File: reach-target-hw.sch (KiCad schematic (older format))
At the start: 37 parts, among them U1 nRF51822-QF, X1 16MHz 40ppm, X2 32.768kHz 20ppm

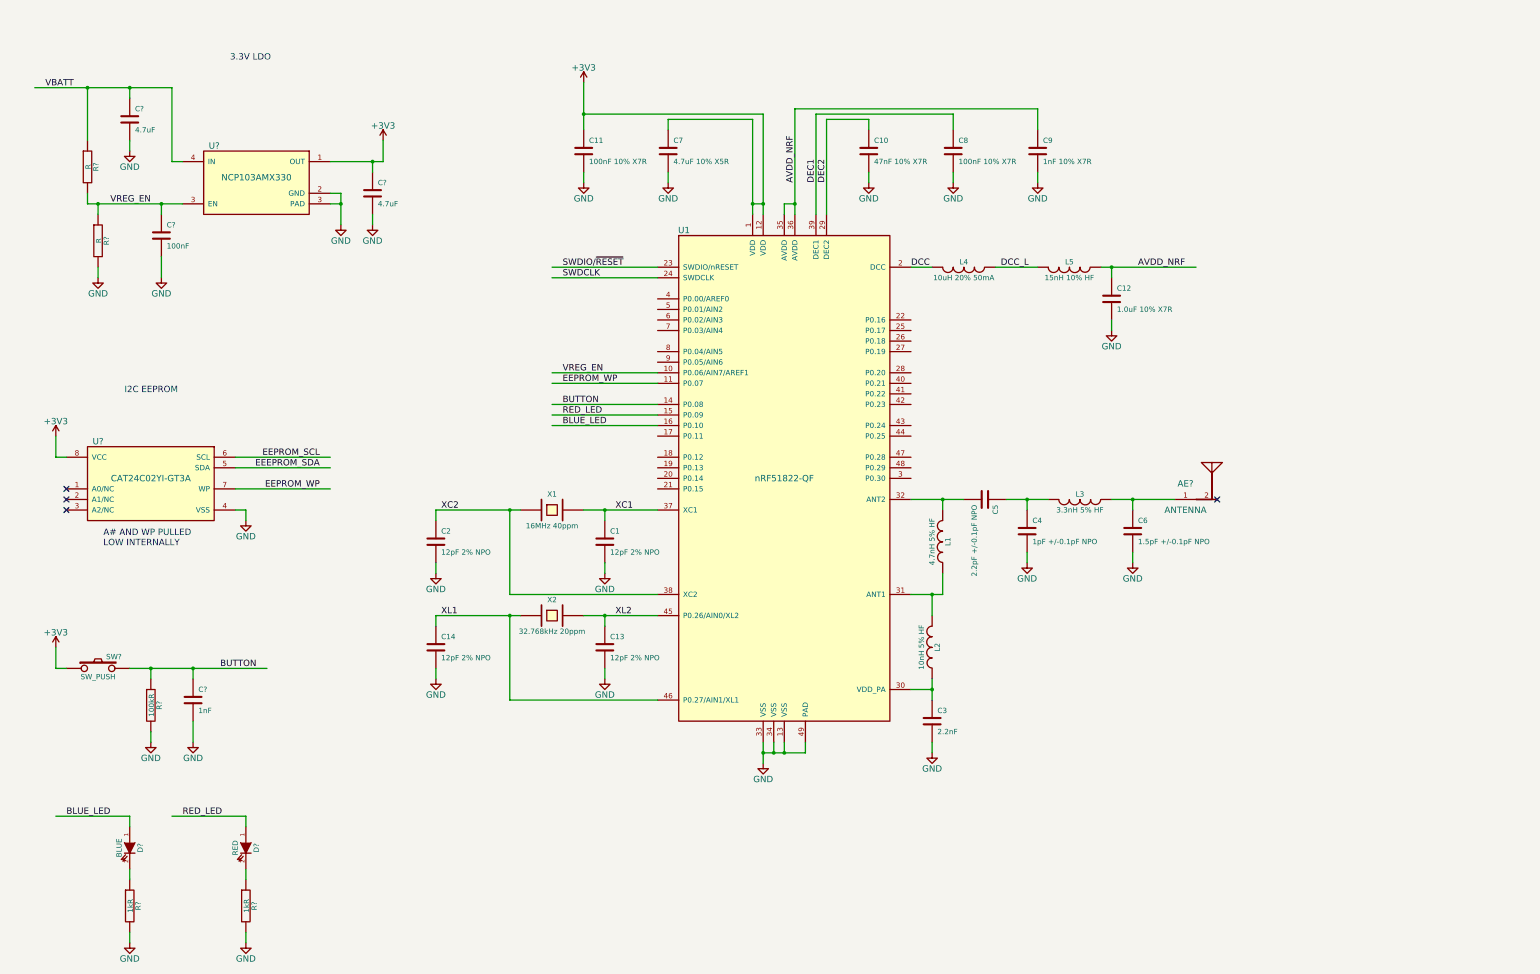
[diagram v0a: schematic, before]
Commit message: added swd/cortex debug pinout. related: none of the nordic reference designs are useful...stupid debugger/usb-to-serial micros are in the way.
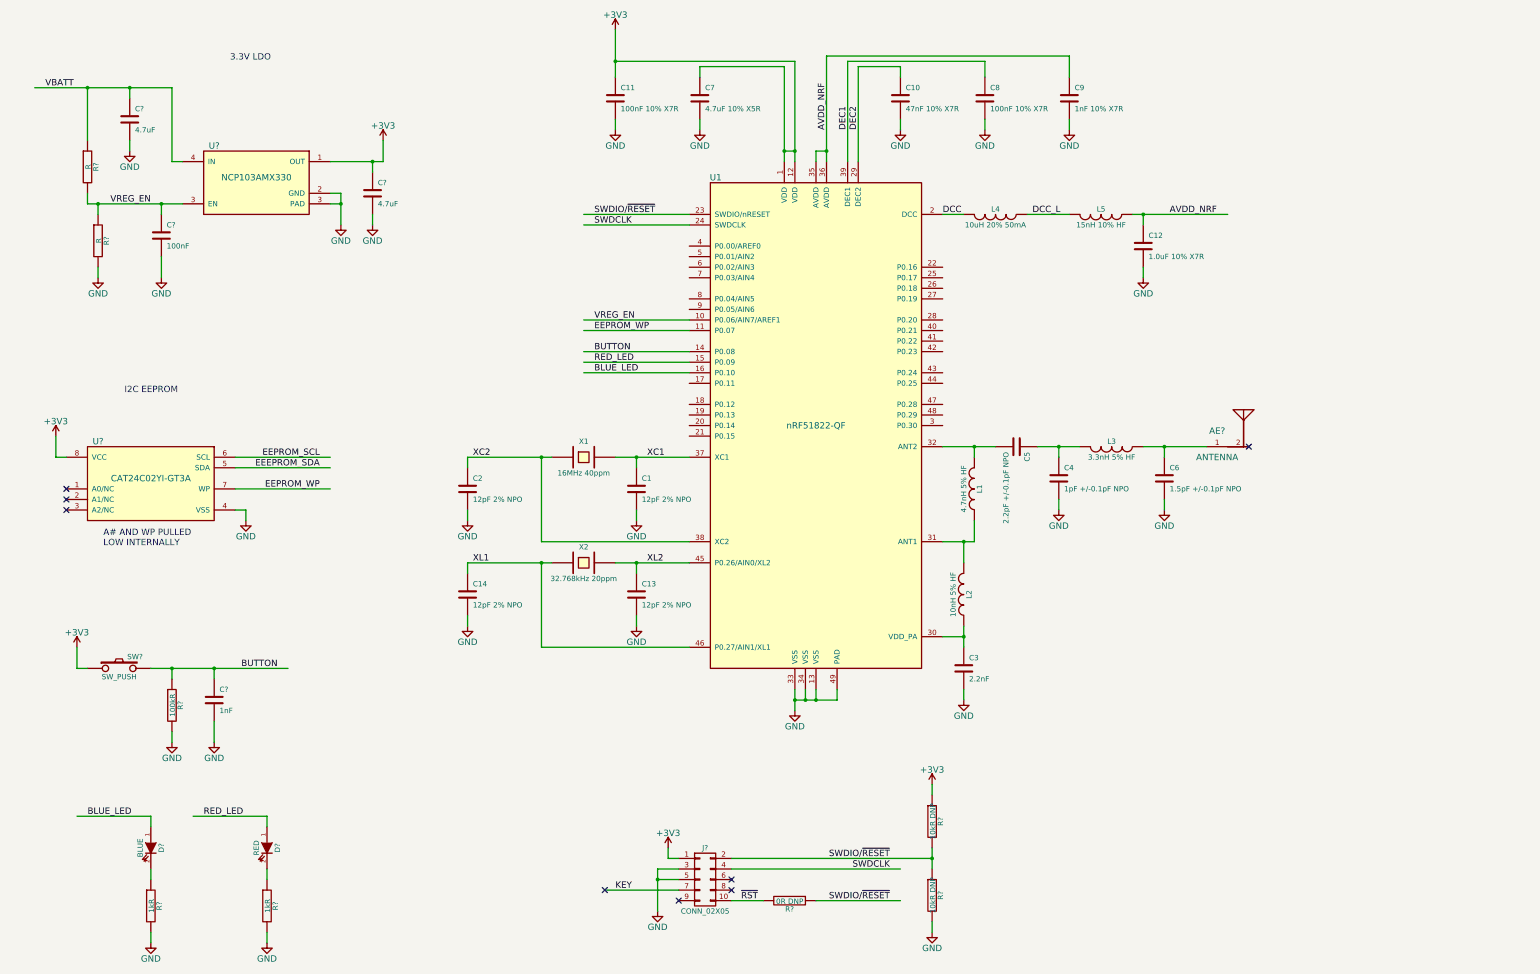
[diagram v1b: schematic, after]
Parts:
- added J?: CONN_02X05, symbol CONN_02X05
- added R?: 0R DNP, symbol R
- added R? (x2): 10kR DNP, symbol R
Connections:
- net labels added: KEY, ~RST
- wire segments 136 -> 124
- no-connect marks 4 -> 8
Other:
- moved on the sheet: AE?, C1, C10, C11, C12, C13, C14, C2, C3, C4, C5, C6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

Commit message: module ports and pps
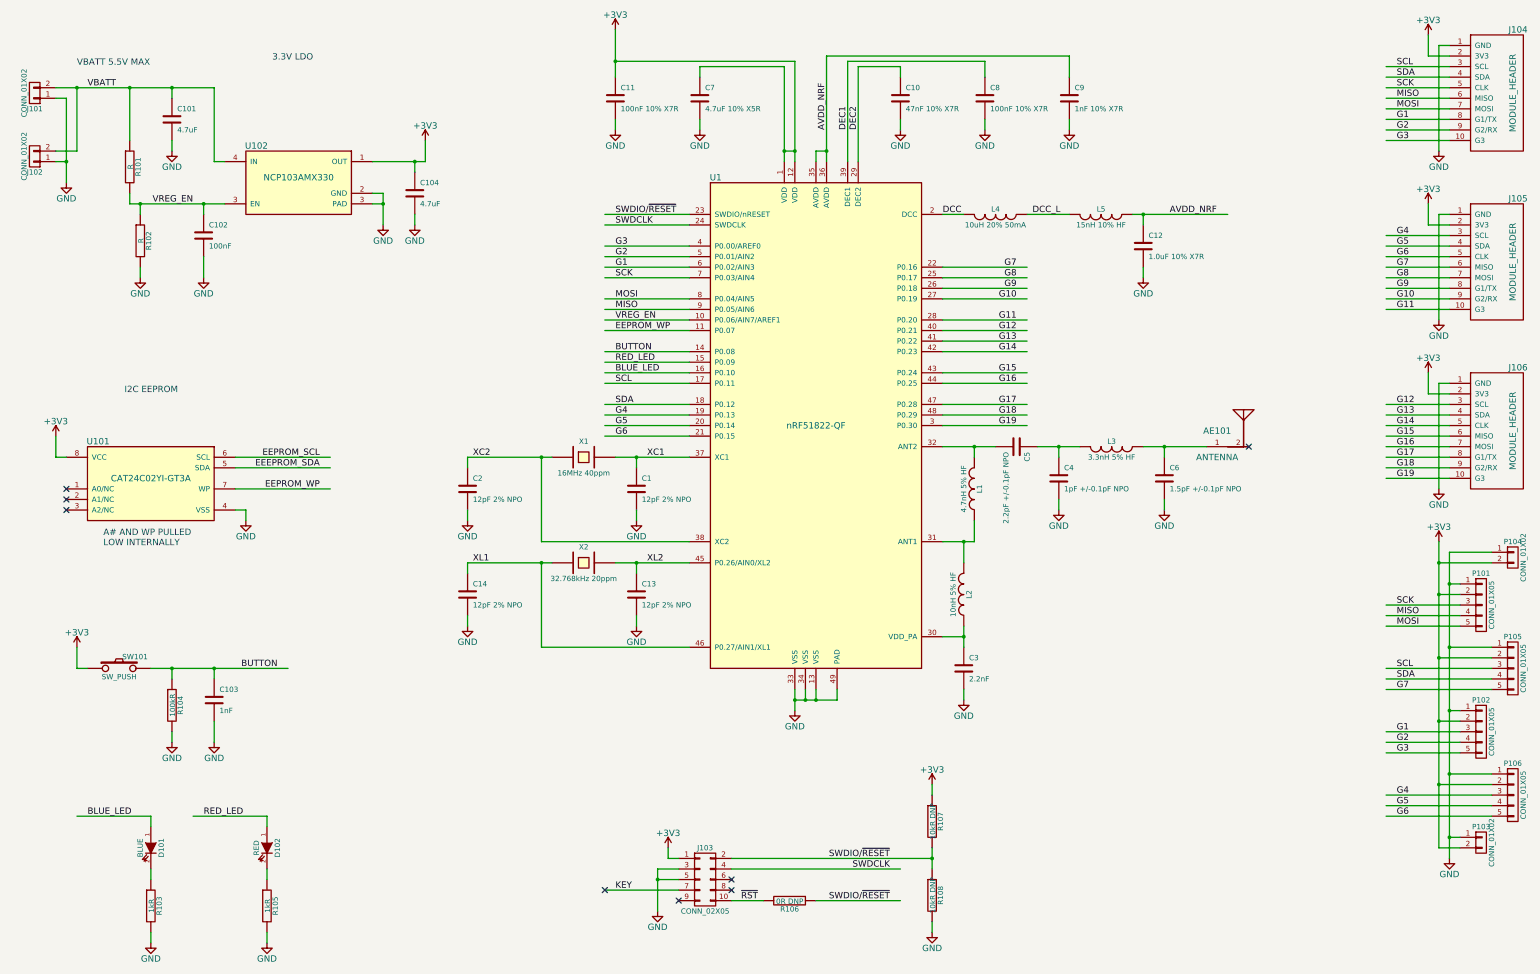
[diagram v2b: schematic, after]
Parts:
- added J101, J102, P103, P104: CONN_01X02, symbol CONN_01X02
- added J104, J105, J106: MODULE_HEADER, symbol MODULE_HEADER
- added P101, P102, P105, P106: CONN_01X05, symbol CONN_01X05
- gave numbers to parts that had none: 19
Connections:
- net labels added: G1, G10, G11, G12, G13, G14, G15, G16, G17, G18, G19, G2, G3, G4, G5, G6, G7, G8, G9, MISO, MOSI, SCK, SCL, SDA
- wire segments 124 -> 254
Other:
- note added: "VBATT 5.5V MAX"
- moved on the sheet: C101, C102, C104, R101, R102, U102

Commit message: nelist and comment about spice sim
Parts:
- R101: value R -> 619kR 1%
- R102: value R -> 100kR 1%
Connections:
- wire segments 254 -> 215
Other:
- note added: "TURNS THE REGULATOR \nOFF AT VBATT = 3V.\nCAN BE OVERRIDEN\nBY GPIO WRITE. SEE\nLTSPICE SCHEMATIC:\nvreg-enable-sim.asc"

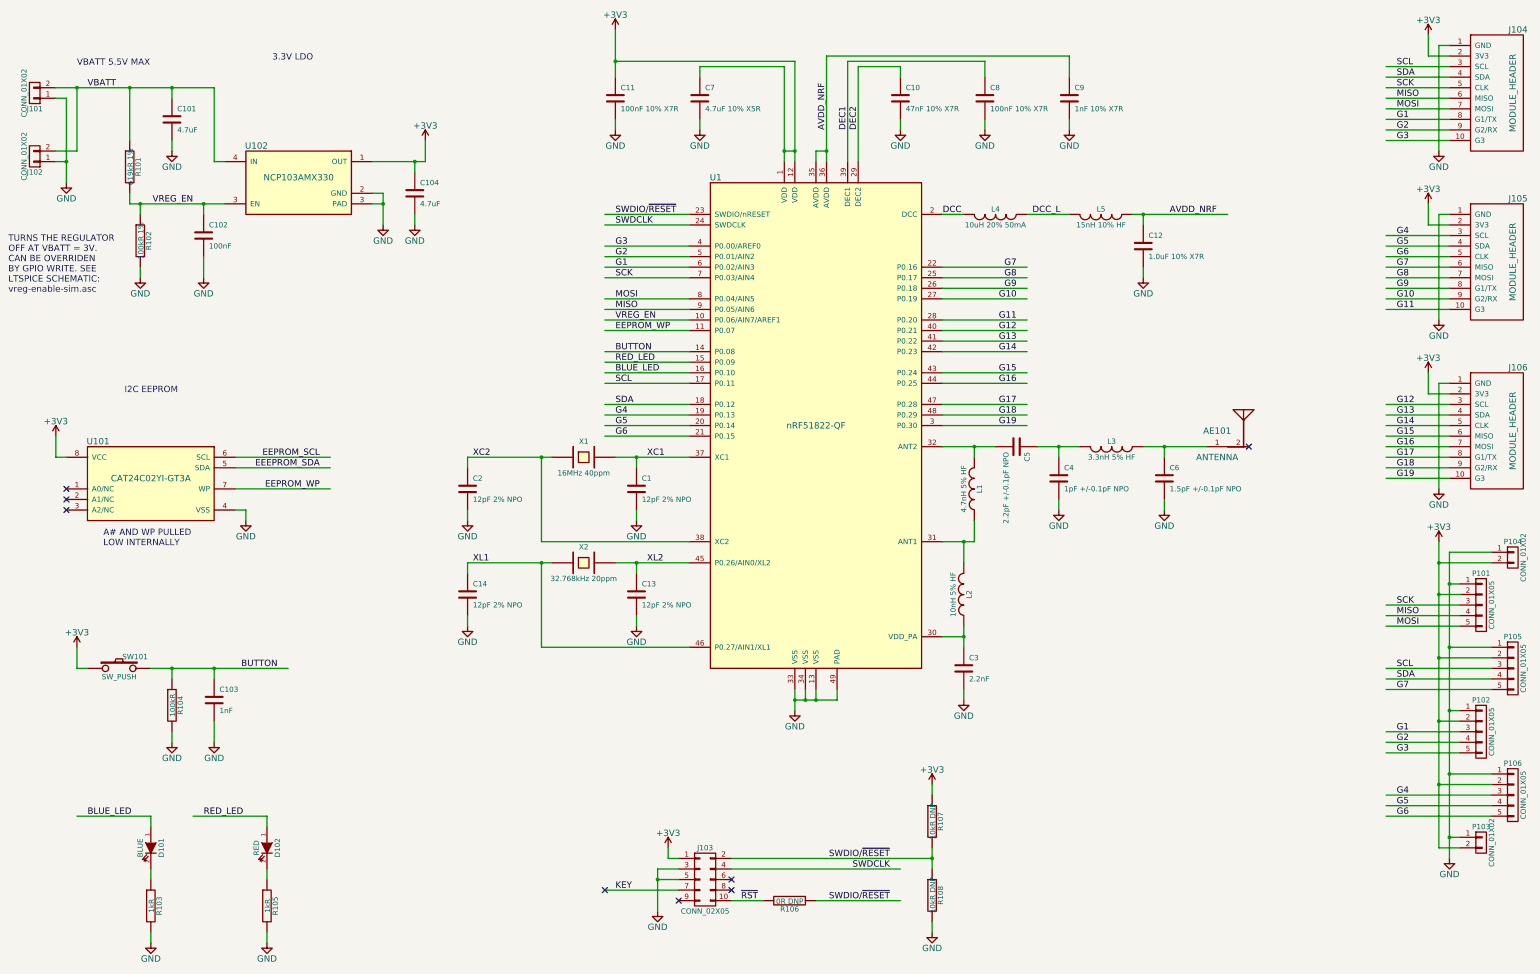
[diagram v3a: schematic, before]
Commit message: pins were reversed
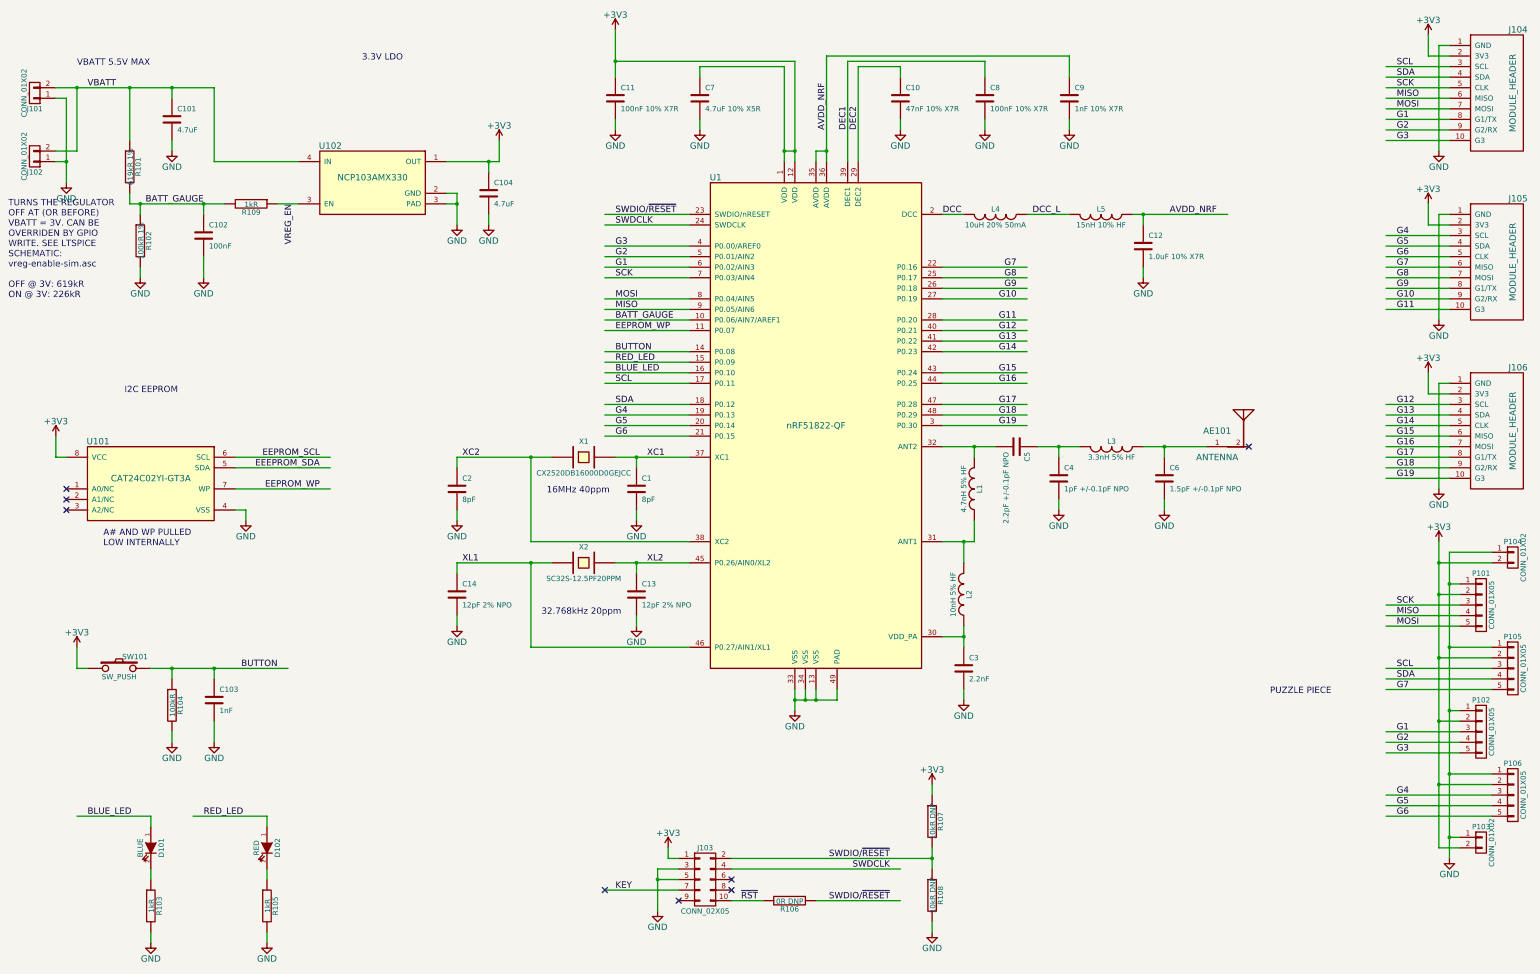
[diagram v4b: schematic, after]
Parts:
- added R109: 1kR, !Parts:SMD-0402, symbol R
- C1, C2: value 12pF 2% NPO -> 8pF; footprint (none) -> !Parts:SMD-0402
- C10, C11, C13, C14, C3, C4, C5, C6, C8, C9, L1, L2, L3, L5, R101, R102, R103, R104, R105, R106, R107, R108: footprint (none) -> !Parts:SMD-0402
- D101, D102: footprint (none) -> LEDs:LED-0603
- J101, J102, SW101: footprint (none) -> Pin_Headers:Pin_Header_Straight_1x02
- J103: footprint (none) -> !Parts:CONN_02x05_0.05in
- J104, J105, J106: footprint (none) -> !Parts:MODULE_HEADER_TESSEL
- P101, P102, P105, P106: footprint (none) -> !Parts:PUZ
- P103, P104: footprint (none) -> !Parts:PUZ_HALF
- U1: footprint (none) -> tm-kicad-lib:QFN-48-1EP
- X1: value 16MHz 40ppm -> CX2520DB16000D0GEJCC
- X2: value 32.768kHz 20ppm -> SC32S-12.5PF20PPM; footprint (none) -> !Parts:FC-135
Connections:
- net labels added: BATT_GAUGE
- wire segments 215 -> 255
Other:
- note added: "16MHz 40ppm"
- note added: "32.768kHz 20ppm"
- note added: "PUZZLE PIECE"
- note added: "TURNS THE REGULATOR \nOFF AT (OR BEFORE)\nVBATT = 3V. CAN BE\nOVERRIDEN BY GPIO\nWRITE. SEE LTSPICE\nSCHEMATIC:\nvreg-enable-sim.asc\n\nOFF @ 3V: 619kR\nON @ 3V: 226kR"
- note removed: "TURNS THE REGULATOR \nOFF AT VBATT = 3V.\nCAN BE OVERRIDEN\nBY GPIO WRITE. SEE\nLTSPICE SCHEMATIC:\nvreg-enable-sim.asc"
- moved on the sheet: C104, C14, C2, U102
